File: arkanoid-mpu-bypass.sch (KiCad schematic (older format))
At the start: 1 part, among them J1 DIP28

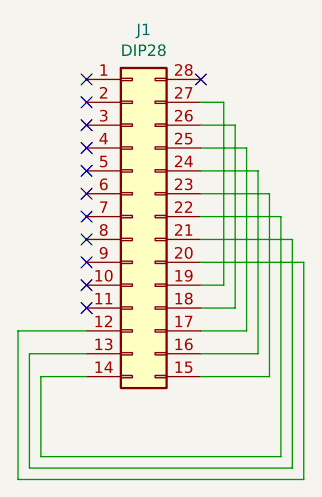
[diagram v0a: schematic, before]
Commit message: Modified to use extra jumper.
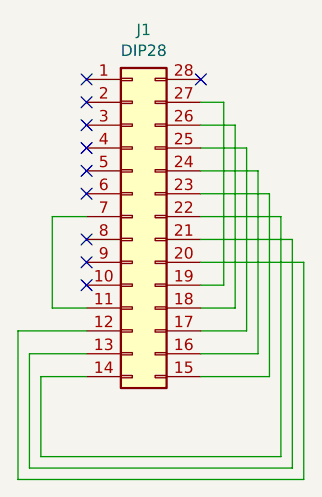
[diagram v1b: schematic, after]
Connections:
- net at J1.11 (Pin_11): now also J1.7 (Pin_7)
- no-connect marks 12 -> 10
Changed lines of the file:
@@
 Sheet 1 1
 Title "Arkanoid MCU Bypass"
-Date "2022-07-09"
-Rev "1.0"
+Date "2022-07-13"
+Rev "1.1"
 Comp "Marc Deslauriers"
 Comment1 ""
@@
 NoConn ~ 5200 2600
 NoConn ~ 5200 2700
-NoConn ~ 5200 2800
 NoConn ~ 5200 2900
 NoConn ~ 5200 3000
 NoConn ~ 5200 3100
-NoConn ~ 5200 3200
 NoConn ~ 5700 2200
+Wire Wire Line
+	5200 2800 5050 2800
+Wire Wire Line
+	5050 2800 5050 3200
+Wire Wire Line
+	5050 3200 5200 3200
 $EndSCHEMATC
